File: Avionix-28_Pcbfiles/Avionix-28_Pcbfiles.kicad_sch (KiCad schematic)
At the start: 1 part, among them J1 Conn_01x02_Pin

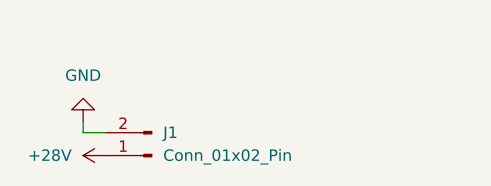
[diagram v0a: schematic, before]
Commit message: ic for buck operation + datasheet inclusion
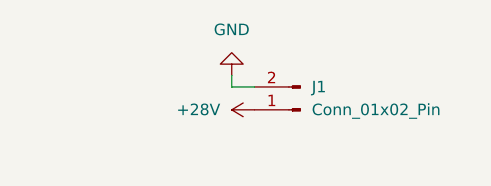
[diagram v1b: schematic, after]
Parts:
- J1: footprint (none) -> Avionix_fprints:CUI_TB007-508-02BE
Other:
- moved on the sheet: J1
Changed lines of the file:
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@@
 	(wire
 		(pts
-			(xy 68.58 83.82) (xy 68.58 85.09)
+			(xy 85.09 78.74) (xy 85.09 80.01)
 		)
 		(stroke
@@
 	(wire
 		(pts
-			(xy 68.58 85.09) (xy 71.12 85.09)
+			(xy 85.09 80.01) (xy 87.63 80.01)
 		)
 		(stroke
@@
 	(symbol
 		(lib_id "Connector:Conn_01x02_Pin")
-		(at 76.2 87.63 180)
+		(at 92.71 82.55 180)
 		(unit 1)
 		(body_style 1)
@@
 		(fields_autoplaced yes)
 		(property "Reference" "J1"
-			(at 77.47 85.0899 0)
+			(at 93.98 80.0099 0)
 			(show_name no)
 			(do_not_autoplace no)
@@
 		)
 		(property "Value" "Conn_01x02_Pin"
-			(at 77.47 87.6299 0)
+			(at 93.98 82.5499 0)
 			(show_name no)
 			(do_not_autoplace no)
@@
 			)
 		)
-		(property "Footprint" ""
-			(at 76.2 87.63 0)
+		(property "Footprint" "Avionix_fprints:CUI_TB007-508-02BE"
+			(at 92.71 82.55 0)
 			(hide yes)
 			(show_name no)
@@
 		)
 		(property "Datasheet" ""
-			(at 76.2 87.63 0)
+			(at 92.71 82.55 0)
 			(hide yes)
 			(show_name no)
@@
 		)
 		(property "Description" "Generic connector, single row, 01x02, script generated"
-			(at 76.2 87.63 0)
+			(at 92.71 82.55 0)
 			(hide yes)
 			(show_name no)
@@
 	(symbol
 		(lib_id "power:GND")
-		(at 68.58 83.82 180)
+		(at 85.09 78.74 180)
 		(unit 1)
 		(body_style 1)
@@
 		(fields_autoplaced yes)
 		(property "Reference" "#PWR01"
-			(at 68.58 77.47 0)
+			(at 85.09 72.39 0)
 			(hide yes)
 			(show_name no)
@@
 		)
 		(property "Value" "GND"
-			(at 68.58 78.74 0)
+			(at 85.09 73.66 0)
 			(show_name no)
 			(do_not_autoplace no)
@@
 		)
 		(property "Footprint" ""
-			(at 68.58 83.82 0)
+			(at 85.09 78.74 0)
 			(hide yes)
 			(show_name no)
@@
 		)
 		(property "Datasheet" ""
-			(at 68.58 83.82 0)
+			(at 85.09 78.74 0)
 			(hide yes)
 			(show_name no)
@@
 		)
 		(property "Description" "Power symbol creates a global label with name \"GND\" , ground"
-			(at 68.58 83.82 0)
+			(at 85.09 78.74 0)
 			(hide yes)
 			(show_name no)
@@
 	(symbol
 		(lib_id "power:+5V")
-		(at 71.12 87.63 90)
+		(at 87.63 82.55 90)
 		(unit 1)
 		(body_style 1)
@@
 		(fields_autoplaced yes)
 		(property "Reference" "#PWR02"
-			(at 74.93 87.63 0)
+			(at 91.44 82.55 0)
 			(hide yes)
 			(show_name no)
@@
 		)
 		(property "Value" "+28V"
-			(at 67.31 87.6299 90)
+			(at 83.82 82.5499 90)
 			(show_name no)
 			(do_not_autoplace no)
@@
 		)
 		(property "Footprint" ""
-			(at 71.12 87.63 0)
+			(at 87.63 82.55 0)
 			(hide yes)
 			(show_name no)
@@
 		)
 		(property "Datasheet" ""
-			(at 71.12 87.63 0)
+			(at 87.63 82.55 0)
 			(hide yes)
 			(show_name no)
@@
 		)
 		(property "Description" "Power symbol creates a global label with name \"+5V\""
-			(at 71.12 87.63 0)
-			(hide yes)
-			(show_name no)
+			(at 87.63 82.55 0)
+			(hide yes)
+			(show_name no)

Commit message: added symbols and fprint for buck
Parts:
- added U1: PTPS561300DDCR, DDC0006A-IPC_A, symbol Avionix-28_symbols:PTPS561300DDCR
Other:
- moved on the sheet: J1
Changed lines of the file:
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@@
 	(wire
 		(pts
-			(xy 85.09 78.74) (xy 85.09 80.01)
+			(xy 77.47 59.69) (xy 77.47 60.96)
 		)
 		(stroke
@@
 	(wire
 		(pts
-			(xy 85.09 80.01) (xy 87.63 80.01)
+			(xy 77.47 60.96) (xy 80.01 60.96)
 		)
 		(stroke
@@
 	)
 	(symbol
+		(lib_id "Avionix-28_symbols:PTPS561300DDCR")
+		(at 137.16 64.77 0)
+		(unit 1)
+		(body_style 1)
+		(exclude_from_sim no)
+		(in_bom yes)
+		(on_board yes)
+		(in_pos_files yes)
+		(dnp no)
+		(fields_autoplaced yes)
+		(property "Reference" "U1"
+			(at 154.94 54.61 0)
+			(show_name no)
+			(do_not_autoplace no)
+			(effects
+				(font
+					(size 1.524 1.524)
+				)
+			)
+		)
+		(property "Value" "PTPS561300DDCR"
+			(at 154.94 57.15 0)
+			(show_name no)
+			(do_not_autoplace no)
+			(effects
+				(font
+					(size 1.524 1.524)
+				)
+			)
+		)
+		(property "Footprint" "DDC0006A-IPC_A"
+			(at 137.16 64.77 0)
+			(hide yes)
+			(show_name no)
+			(do_not_autoplace no)
+			(effects
+				(font
+					(size 1.27 1.27)
+					(italic yes)
+				)
+			)
+		)
+		(property "Datasheet" "https://www.ti.com/lit/gpn/tps561300"
+			(at 137.16 64.77 0)
+			(hide yes)
+			(show_name no)
+			(do_not_autoplace no)
+			(effects
+				(font
+					(size 1.27 1.27)
+					(italic yes)
+				)
+			)
+		)
+		(property "Description" ""
+			(at 137.16 64.77 0)
+			(hide yes)
+			(show_name no)
+			(do_not_autoplace no)
+			(effects
+				(font
+					(size 1.27 1.27)
+				)
+			)
+		)
+		(pin "3"
+		)
+		(pin "2"
+		)
+		(pin "4"
+		)
+		(pin "1"
+		)
+		(pin "6"
+		)
+		(pin "5"
+		)
+		(instances
+			(project "Avionix-28_Pcbfiles"
+				(path "/c5efffa8-e950-4f99-a1ea-77b4665bba5b"
+					(reference "U1")
+					(unit 1)
+				)
+			)
+		)
+	)
+	(symbol
 		(lib_id "Connector:Conn_01x02_Pin")
-		(at 92.71 82.55 180)
+		(at 85.09 63.5 180)
 		(unit 1)
 		(body_style 1)
@@
 		(fields_autoplaced yes)
 		(property "Reference" "J1"
-			(at 93.98 80.0099 0)
+			(at 86.36 60.9599 0)
 			(show_name no)
 			(do_not_autoplace no)
@@
 		)
 		(property "Value" "Conn_01x02_Pin"
-			(at 93.98 82.5499 0)
+			(at 86.36 63.4999 0)
 			(show_name no)
 			(do_not_autoplace no)
@@
 		)
 		(property "Footprint" "Avionix_fprints:CUI_TB007-508-02BE"
-			(at 92.71 82.55 0)
+			(at 85.09 63.5 0)
 			(hide yes)
 			(show_name no)
@@
 		)
 		(property "Datasheet" ""
-			(at 92.71 82.55 0)
+			(at 85.09 63.5 0)
 			(hide yes)
 			(show_name no)
@@
 		)
 		(property "Description" "Generic connector, single row, 01x02, script generated"
-			(at 92.71 82.55 0)
+			(at 85.09 63.5 0)
 			(hide yes)
 			(show_name no)
@@
 	(symbol
 		(lib_id "power:GND")
-		(at 85.09 78.74 180)
+		(at 77.47 59.69 180)
 		(unit 1)
 		(body_style 1)
@@
 		(fields_autoplaced yes)
 		(property "Reference" "#PWR01"
-			(at 85.09 72.39 0)
+			(at 77.47 53.34 0)
 			(hide yes)
 			(show_name no)
@@
 		)
 		(property "Value" "GND"
-			(at 85.09 73.66 0)
+			(at 77.47 54.61 0)
 			(show_name no)
 			(do_not_autoplace no)
@@
 		)
 		(property "Footprint" ""
-			(at 85.09 78.74 0)
+			(at 77.47 59.69 0)
 			(hide yes)
 			(show_name no)
@@
 		)
 		(property "Datasheet" ""
-			(at 85.09 78.74 0)
+			(at 77.47 59.69 0)
 			(hide yes)
 			(show_name no)
@@
 		)
 		(property "Description" "Power symbol creates a global label with name \"GND\" , ground"
-			(at 85.09 78.74 0)
+			(at 77.47 59.69 0)
 			(hide yes)
 			(show_name no)
@@
 	(symbol
 		(lib_id "power:+5V")
-		(at 87.63 82.55 90)
+		(at 133.35 63.5 0)
+		(unit 1)
+		(body_style 1)
+		(exclude_from_sim no)
+		(in_bom yes)
+		(on_board yes)
+		(in_pos_files yes)
+		(dnp no)
+		(fields_autoplaced yes)
+		(property "Reference" "#PWR03"
+			(at 133.35 67.31 0)
+			(hide yes)
+			(show_name no)
+			(do_not_autoplace no)
+			(effects
+				(font
+					(size 1.27 1.27)
+				)
+			)
+		)
+		(property "Value" "+28V"
+			(at 133.35 58.42 0)
+			(show_name no)
+			(do_not_autoplace no)
+			(effects
+				(font
+					(size 1.27 1.27)
+				)
+			)
+		)
+		(property "Footprint" ""
+			(at 133.35 63.5 0)
+			(hide yes)
+			(show_name no)
+			(do_not_autoplace no)
+			(effects
+				(font
+					(size 1.27 1.27)
+				)
+			)
+		)
+		(property "Datasheet" ""
+			(at 133.35 63.5 0)
+			(hide yes)
+			(show_name no)
+			(do_not_autoplace no)
+			(effects
+				(font
+					(size 1.27 1.27)
+				)
+			)
+		)
+		(property "Description" "Power symbol creates a global label with name \"+5V\""
+			(at 133.35 63.5 0)
+			(hide yes)
+			(show_name no)
+			(do_not_autoplace no)
+			(effects
+				(font
+					(size 1.27 1.27)
+				)
+			)
+		)
+		(pin "1"
+		)
+		(instances
+			(project "Avionix-28_Pcbfiles"
+				(path "/c5efffa8-e950-4f99-a1ea-77b4665bba5b"
+					(reference "#PWR03")
+					(unit 1)
+				)
+			)
+		)
+	)
+	(symbol
+		(lib_id "power:+5V")
+		(at 80.01 63.5 90)
 		(unit 1)
 		(body_style 1)
@@
 		(fields_autoplaced yes)
 		(property "Reference" "#PWR02"
-			(at 91.44 82.55 0)
+			(at 83.82 63.5 0)
 			(hide yes)
 			(show_name no)
@@
 		)
 		(property "Value" "+28V"
-			(at 83.82 82.5499 90)
+			(at 76.2 63.4999 90)
 			(show_name no)
 			(do_not_autoplace no)
@@
 		)
 		(property "Footprint" ""
-			(at 87.63 82.55 0)
+			(at 80.01 63.5 0)
 			(hide yes)
 			(show_name no)
@@
 		)
 		(property "Datasheet" ""
-			(at 87.63 82.55 0)
+			(at 80.01 63.5 0)
 			(hide yes)
 			(show_name no)
@@
 		)
 		(property "Description" "Power symbol creates a global label with name \"+5V\""
-			(at 87.63 82.55 0)
-			(hide yes)
-			(show_name no)
+			(at 80.01 63.5 0)
+			(hide yes)
+			(show_name no)

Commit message: worked up on sch
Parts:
- added C1, C2, C3: 10u, symbol Device:C
- added C4, C6: 100n, symbol Device:C
- added C7: 75p, symbol Device:C
- added L1: 25u, symbol Device:L
- added R3, R4: 100k, symbol Device:R
- added R5: 13k3, symbol Device:R
- added R6: 0, symbol Device:R
- added TP11: TestPoint, symbol Connector:TestPoint
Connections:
- net +28V: now also U1.3 (VIN), C1.1, C2.1, C3.1, C4.1
- net GND: now also U1.1 (GND), C1.2, C2.2, C3.2, C4.2, R5.1
- net at U1.2 (SW): now also C6.2, L1.1
- net at U1.4 (VOUT): now also C7.1, R4.1, R5.2
- net at U1.6 (BOOT): now also R6.1
- new net: C7.2, R3.1, R4.2, TP11.1
- new net: L1.2, R3.2
- new net: C6.1, R6.2
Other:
- moved on the sheet: J1
